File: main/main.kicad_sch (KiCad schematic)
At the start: 1 part

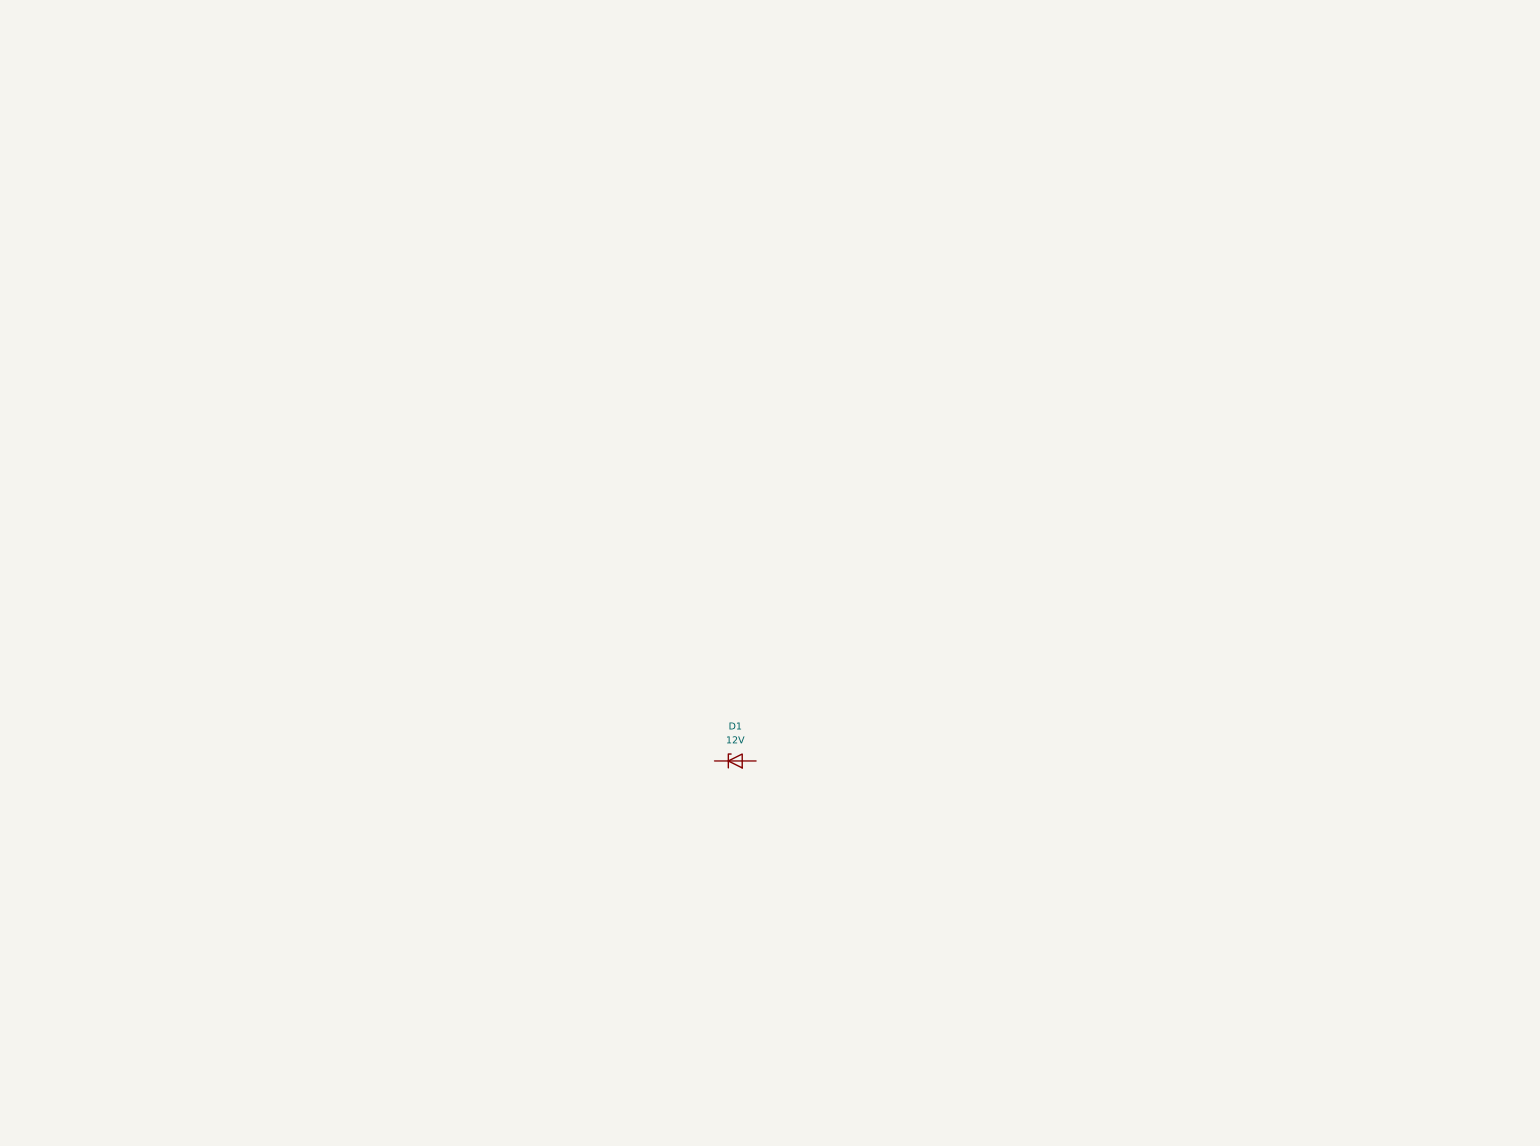
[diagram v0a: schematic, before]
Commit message: merging a pi pico board with low power domain
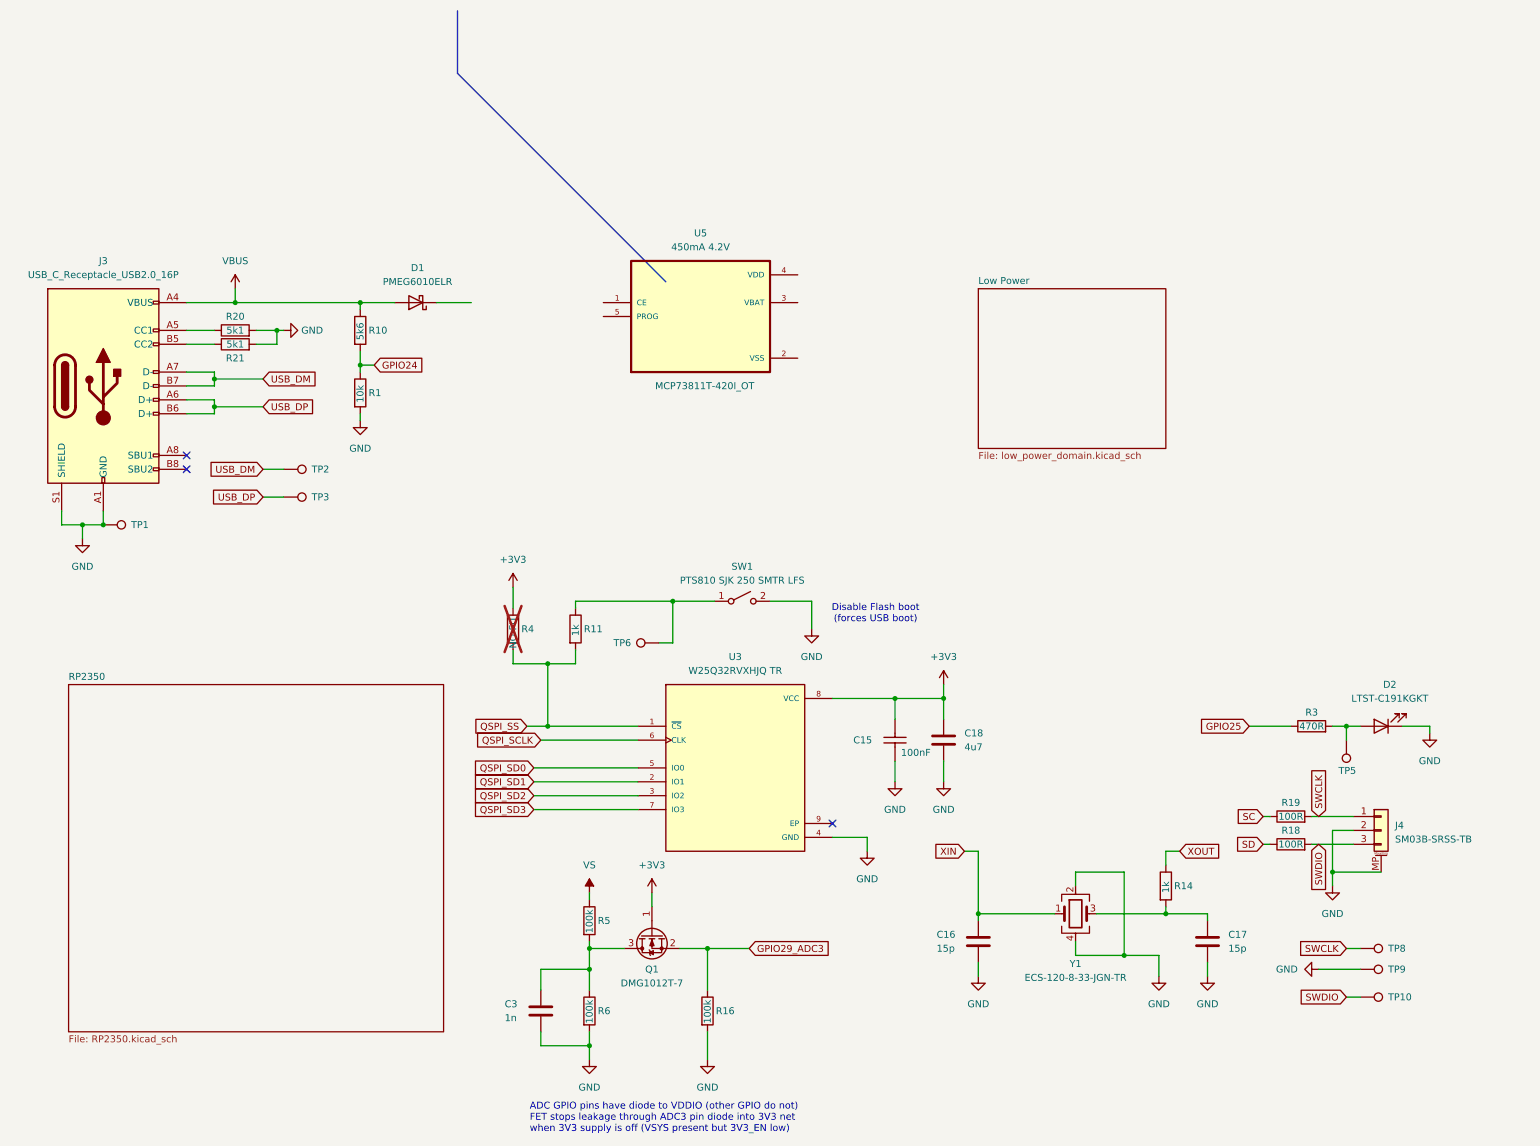
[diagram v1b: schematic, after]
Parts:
- removed D1: 12V, smv_footprints:KICAD_SOT-23-3, symbol smv_diodes:DIOD_ROHM_BZX84B12VLYFHT116
- added C15: 100NF_0201_10V_X7R, smv_footprints:C_0201_0603Metric, symbol smv_capacitors:100NF_0201_10V_X7R
- added C16, C17: 15p, Capacitor_SMD:C_0201_0603Metric, symbol Device:C
- added C18: 4u7, Capacitor_SMD:C_0402_1005Metric, symbol Device:C
- added C3: 1n, Capacitor_SMD:C_0201_0603Metric, symbol Device:C
- added D1: PMEG6010ELR, Diode_SMD:D_SOD-123F, symbol Device:D_Schottky
- added D2: LTST-C191KGKT, LED_SMD:LED_0603_1608Metric, symbol Device:LED
- added J3: USB_C_Receptacle_USB2.0_16P, Connector_USB:USB_C_Receptacle_GCT_USB4105-xx-A_16P_TopMnt_Horizontal, symbol Connector:USB_C_Receptacle_USB2.0_16P
- added J4: SM03B-SRSS-TB, Connector_JST:JST_SH_SM03B-SRSS-TB_1x03-1MP_P1.00mm_Horizontal, symbol Connector_Generic_MountingPin:Conn_01x03_MountingPin
- added Q1: DMG1012T-7, Package_TO_SOT_SMD:SOT-523, symbol Device:Q_NMOS_GSD
- added R1: 10k, Resistor_SMD:R_0201_0603Metric, symbol Device:R
- added R10: 5k6, Resistor_SMD:R_0201_0603Metric, symbol Device:R
- added R11, R14: 1k, Resistor_SMD:R_0201_0603Metric, symbol Device:R
- added R16, R5, R6: 100k, Resistor_SMD:R_0201_0603Metric, symbol Device:R
- added R18, R19: 100R, Resistor_SMD:R_0201_0603Metric, symbol Device:R
- added R20, R21: 5k1, Resistor_SMD:R_0402_1005Metric, symbol Device:R
- added R3: 470R, Resistor_SMD:R_0201_0603Metric, symbol Device:R
- added R4: NO-FIT, Resistor_SMD:R_0201_0603Metric, symbol Device:R
- added SW1: PTS810 SJK 250 SMTR LFS, Button_Switch_SMD:SW_SPST_PTS810, symbol Switch:SW_SPST
- added TP1, TP10, TP2, TP3, TP5, TP6, TP8, TP9: TestPoint, TestPoint:TestPoint_Pad_1.5x1.5mm, symbol Connector:TestPoint
- added U3: W25Q32RVXHJQ TR, Package_DFN_QFN:TDFN-8-1EP_3x2mm_P0.5mm_EP1.3x1.4mm, symbol Pico 2 C:W25Q16JVUXIQ TR
- added U5: 450mA 4.2V, smv_footprints:SOT95P280X145-5N, symbol smv_ic:IC_MICROCHIP_MCP73811T-420I_OT
- added Y1: ECS-120-8-33-JGN-TR, Crystal:Crystal_SMD_SeikoEpson_FA238-4Pin_3.2x2.5mm, symbol Device:Crystal_GND24
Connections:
- new net: R11.1, SW1.1 (A), TP6.1
- new net: C17.1, R14.2, Y1.3
- new net: C3.1, Q1.3 (D), R5.2, R6.1
- new net: D2.2 (A), R3.2, TP5.1
- new net: J3.A5 (CC1), R20.1
- new net: J3.B5 (CC2), R21.1
- new net +3V3: C15.1, C18.1, Q1.1 (G), R4.1, U3.8 (VCC)
- new net GND: C15.2, C16.2, C17.2, C18.2, C3.2, D2.1 (K), J3.A1 (GND), J3.A12 (GND), J3.B1 (GND), J3.B12 (GND), J3.S1 (SHIELD), J4.2 (Pin_2), J4.MP (MountPin), R1.2, R16.2, R20.2, R21.2, R6.2, SW1.2 (B), TP1.1, TP9.1, U3.4 (GND), Y1.2, Y1.4
- new net GPIO24: R1.1, R10.2
- new net GPIO25: R3.1
- new net GPIO29_ADC3: Q1.2 (S), R16.1
- new net QSPI_SCLK: U3.6 (CLK)
- new net QSPI_SD0: U3.5 (IO0)
- new net QSPI_SD1: U3.2 (IO1)
- new net QSPI_SD2: U3.3 (IO2)
- new net QSPI_SD3: U3.7 (IO3)
- new net QSPI_SS: R11.2, R4.2, U3.1 (~{CS})
- new net SC: R19.1
- new net SD: R18.1
- new net SWCLK: J4.1 (Pin_1), R19.2, TP8.1
- new net SWDIO: J4.3 (Pin_3), R18.2, TP10.1
- new net USB_DM: J3.A7 (D-), J3.B7 (D-), TP2.1
- new net USB_DP: J3.A6 (D+), J3.B6 (D+), TP3.1
- new net VBUS: D1.2 (A), J3.A4 (VBUS), J3.A9 (VBUS), J3.B4 (VBUS), J3.B9 (VBUS), R10.1
- new net VS: R5.1
- new net XIN: C16.1, Y1.1
- new net XOUT: R14.1
- no-connect marks 0 -> 3
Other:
- added sheet Low Power (low_power_domain.kicad_sch)
- added sheet RP2350 (RP2350.kicad_sch)
- note added: "ADC GPIO pins have diode to VDDIO (other GPIO do not) FET stops leakage through ADC3 pin diode into 3V3 net when 3V3 supply is off (VSYS present but 3V3_EN low)"
- note added: "Disable Flash boot (forces USB boot)"
- company: smoov dev ab -> Carlos Sabogal
- title: MAIN -> project piCo 2

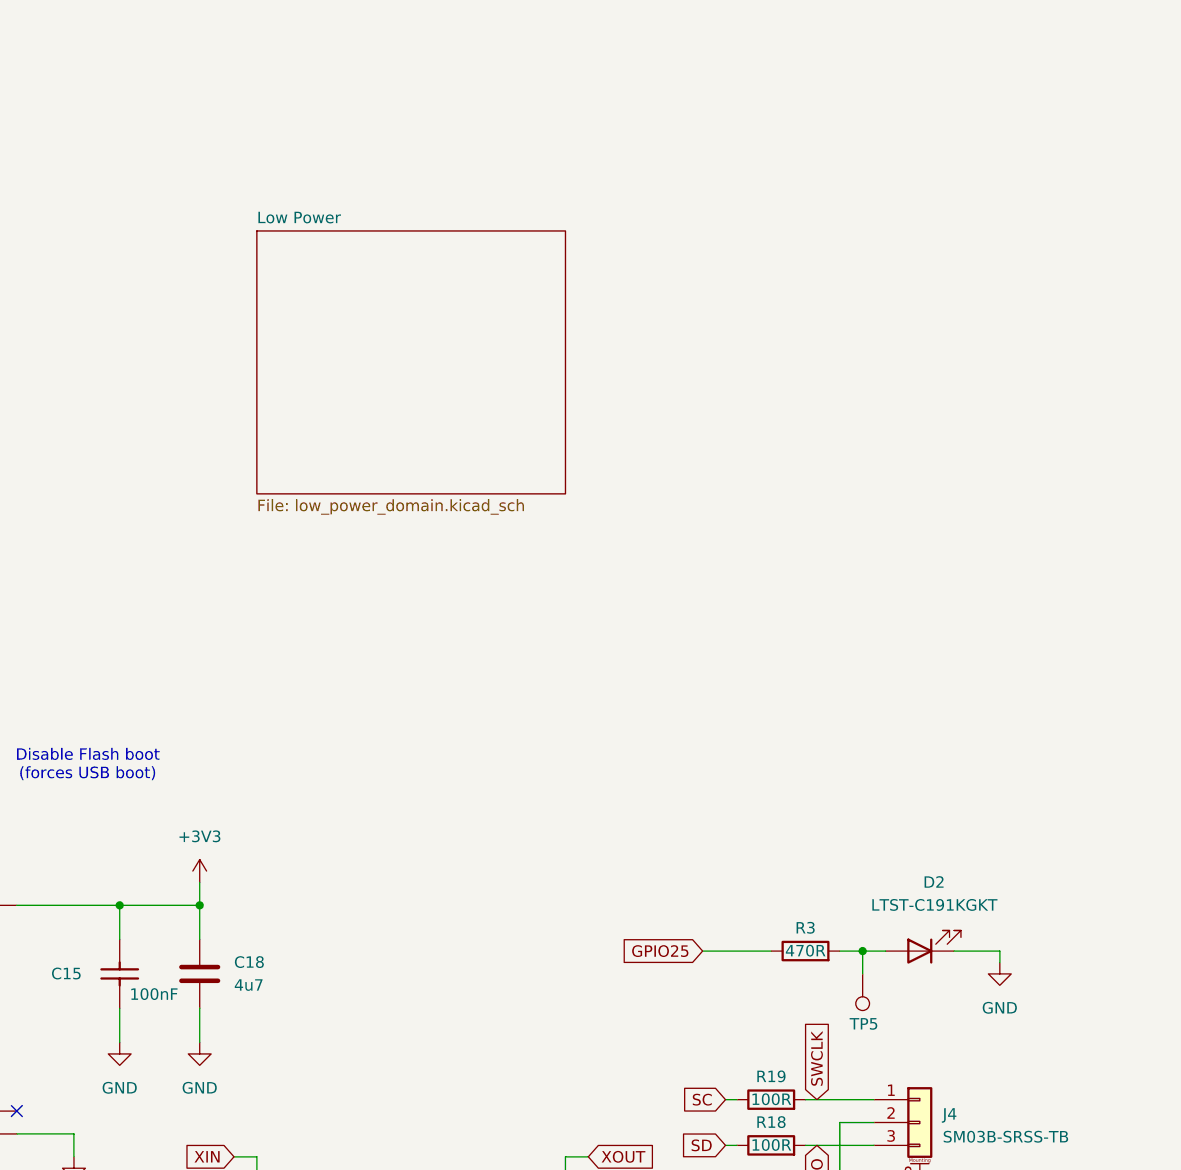
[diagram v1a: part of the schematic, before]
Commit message: last commit with pi-pico still on
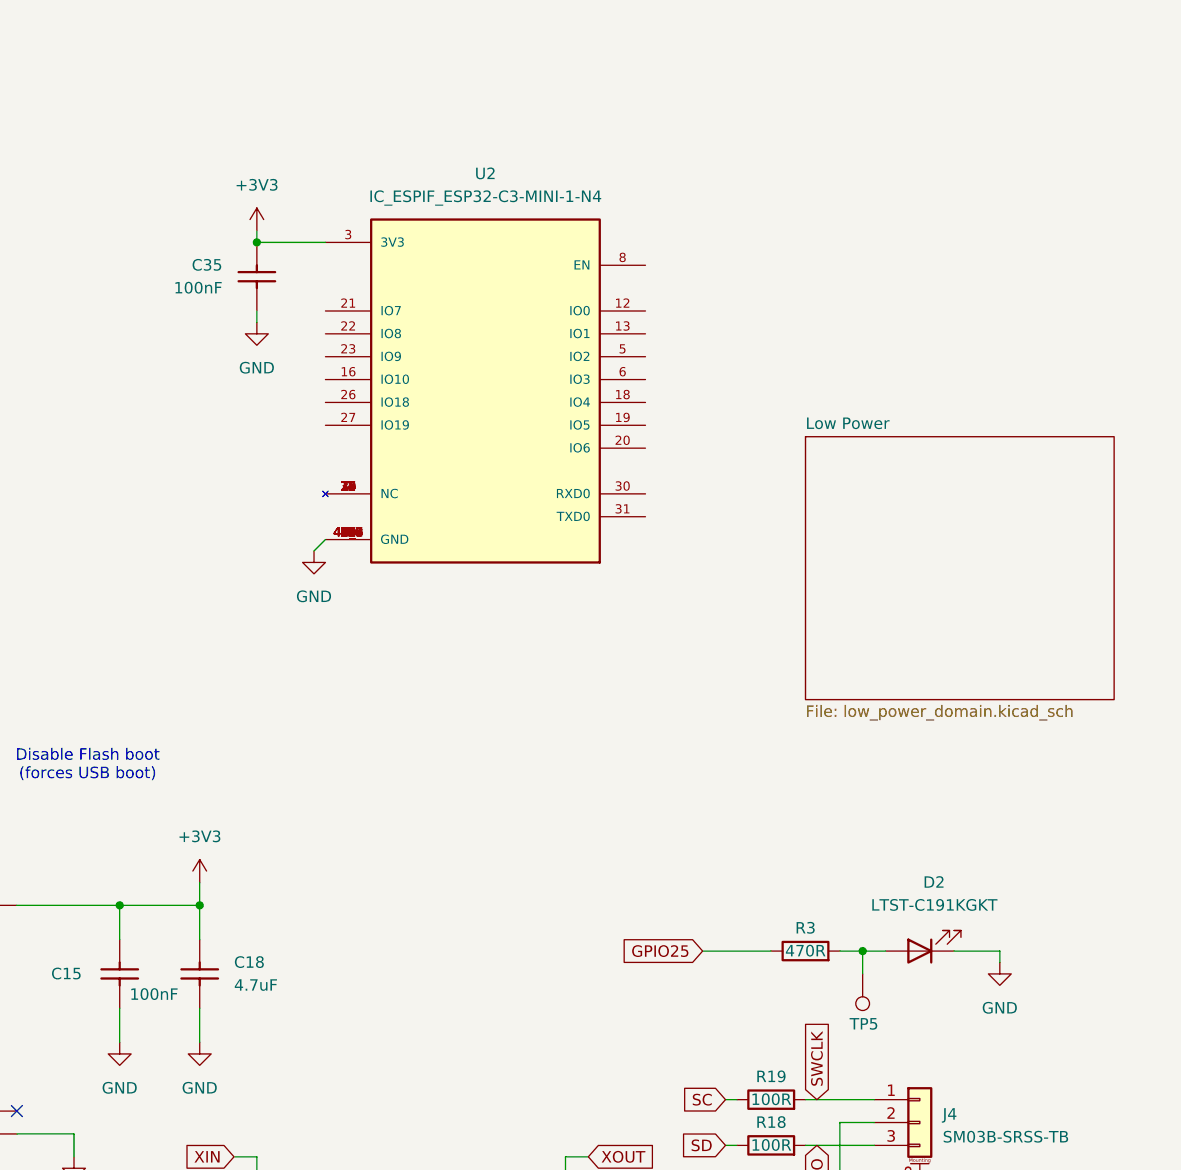
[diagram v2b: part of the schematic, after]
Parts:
- added C35: 100NF_0201_10V_X7R, smv_footprints:C_0201_0603Metric, symbol smv_capacitors:100NF_0201_10V_X7R
- added U2: IC_ESPIF_ESP32-C3-MINI-1-N4, smv_footprints:IC_ESPIF_ESP32-C3-MINI-1-N4, symbol smv_ic:IC_ESPIF_ESP32-C3-MINI-1-N4
- C18: value 4u7 -> 4.7UF 0402 10V X7R; footprint Capacitor_SMD:C_0402_1005Metric -> smv_footprints:C_0402_1005Metric; symbol Device:C -> smv_capacitors:4.7UF_0402_10V_X7R; Voltage (none) -> 0V; manf (none) -> Generic; manfn# (none) -> Generic; val (none) -> 4.7uF
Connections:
- net +3V3: now also C35.1, U2.3 (3V3)
- net GND: now also C35.2, U2.1 (GND), U2.11 (GND), U2.14 (GND), U2.2 (GND), U2.36 (GND), U2.37 (GND), U2.38 (GND), U2.39 (GND), U2.40 (GND), U2.41 (GND), U2.42 (GND), U2.43 (GND), U2.44 (GND), U2.45 (GND), U2.46 (GND), U2.47 (GND), U2.48 (GND), U2.49_1 (GND), U2.49_2 (GND), U2.49_3 (GND), U2.49_4 (GND), U2.49_5 (GND), U2.49_6 (GND), U2.49_7 (GND), U2.49_8 (GND), U2.49_9 (GND), U2.50 (GND), U2.51 (GND), U2.52 (GND), U2.53 (GND)
- new net: U2.10 (NC), U2.15 (NC), U2.17 (NC), U2.24 (NC), U2.25 (NC), U2.28 (NC), U2.29 (NC), U2.32 (NC), U2.33 (NC), U2.34 (NC), U2.35 (NC), U2.4 (NC), U2.7 (NC), U2.9 (NC)
